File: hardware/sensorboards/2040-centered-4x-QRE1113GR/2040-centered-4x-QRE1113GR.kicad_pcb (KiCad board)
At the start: 2 copper layers, 49 x 46.5 mm, 15 parts, among them J1 Conn_01x10_Male, U1 QRE1113GR, U2 QRE1113GR, U3 QRE1113GR, U4 QRE1113GR

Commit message: removed extrusion which has nothing to do here in KiCad, will use OpenSCAD for rendering
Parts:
- removed ?: , 
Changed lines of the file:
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@@
       (net 11 "Net-(TP2-Pad1)") (pinfunction "1") (pintype "passive"))
-  )
-  (footprint "" (layer "F.Cu")
-    (at 168.1 92.1)
-    (fp_text reference "" (at 0 0) (layer "F.SilkS")
-      (effects (font (size 1.27 1.27) (thickness 0.15)))
-    )
-    (fp_text value "" (at 0 0) (layer "F.SilkS")
-      (effects (font (size 1.27 1.27) (thickness 0.15)))
-    )
-    (pad "" np_thru_hole circle (at 0 0) (size 3.2 3.2) (drill 3.2) (layers *.Cu *.Mask))
-    (model "/home/davide/repo/github/piano-conversion-davide/HFS5-4040-100.stp"
-      (offset (xyz -75 0 -22))
-      (scale (xyz 1 1 1))
-      (rotate (xyz 0 90 0))
-    )
   )
   (footprint "Mounting_Holes:MountingHole_3.2mm_M3" (layer "F.Cu")

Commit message: larger board for back action
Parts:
- moved J1 6.20 mm to (150.0, 62.1)
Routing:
- net /C4: track 28.9 -> 35.7 mm
- net Net-(U2-Pad3): track 27.6 -> 34.3 mm
- net /POS: track 39.3 -> 45.8 mm
- net /E3: track 27.6 -> 34.1 mm
- net /E2: track 24.6 -> 30.8 mm
- net /E1: track 28.9 -> 35.1 mm
- net /NEG: track 39.1 -> 45.2 mm
- net /C3: track 24.7 -> 30.8 mm
- net /C1: track 28.3 -> 34.0 mm
- net /E4: track 28.4 -> 34.0 mm
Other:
- board size 49 x 46.5 mm -> 49 x 52 mm
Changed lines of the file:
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@@
   )
   (footprint "Connector_PinHeader_2.54mm:PinHeader_1x10_P2.54mm_Vertical" (layer "B.Cu")
-    (at 149.96 68.3 90)
+    (at 149.96 62.1 90)
     (descr "Through hole straight pin header, 1x10, 2.54mm pitch, single row")
     (tags "Through hole pin header THT 1x10 2.54mm single row")
@@
     )
   )
-  (gr_rect (start 114 65.5) (end 163 112) (layer "Edge.Cuts") (width 0.05) (fill none))
-  (segment (start 149.96 68.3) (end 162 68.3) (width 1) (layer "F.Cu") (net 1))
-  (segment (start 162 68.3) (end 162 91) (width 1) (layer "F.Cu") (net 1))
-  (segment (start 162 91) (end 162 92.8) (width 1) (layer "F.Cu") (net 1))
+  (gr_rect (start 114 60) (end 163 112) (layer "Edge.Cuts") (width 0.05) (fill none))
+  (segment (start 162 62.2) (end 162 92.8) (width 1) (layer "F.Cu") (net 1))
+  (segment (start 161.9 62.1) (end 162 62.2) (width 0.25) (layer "F.Cu") (net 1))
+  (segment (start 149.96 62.1) (end 161.9 62.1) (width 1) (layer "F.Cu") (net 1))
   (segment (start 159.5 92.9) (end 161.9 92.9) (width 0.5) (layer "F.Cu") (net 1))
   (segment (start 161.9 92.9) (end 162 92.8) (width 0.5) (layer "F.Cu") (net 1))
-  (segment (start 155.8 90.8) (end 155.8 77.66927) (width 0.5) (layer "F.Cu") (net 2))
-  (segment (start 146.464635 69.884635) (end 144.88 68.3) (width 0.5) (layer "F.Cu") (net 2))
-  (segment (start 155.8 77.66927) (end 148.015365 69.884635) (width 0.5) (layer "F.Cu") (net 2))
-  (segment (start 148.015365 69.884635) (end 146.464635 69.884635) (width 0.5) (layer "F.Cu") (net 2))
-  (segment (start 155.5 91.1) (end 155.8 90.8) (width 0.5) (layer "F.Cu") (net 2))
+  (segment (start 155.8 90.8) (end 155.5 91.1) (width 0.5) (layer "F.Cu") (net 2))
+  (segment (start 155.8 72.4) (end 155.8 90.8) (width 0.5) (layer "F.Cu") (net 2))
+  (segment (start 145.5 62.1) (end 155.8 72.4) (width 0.5) (layer "F.Cu") (net 2))
+  (segment (start 144.88 62.1) (end 145.5 62.1) (width 0.5) (layer "F.Cu") (net 2))
   (segment (start 157.59952 91.1) (end 159.5 91.1) (width 0.5) (layer "F.Cu") (net 3))
-  (segment (start 147.42 68.3) (end 156.49952 77.37952) (width 0.5) (layer "F.Cu") (net 3))
+  (segment (start 156.5 77.37904) (end 156.49952 77.37952) (width 0.5) (layer "F.Cu") (net 3))
+  (segment (start 147.42 62.1) (end 147 62.1) (width 0.5) (layer "F.Cu") (net 3))
   (segment (start 156.49952 77.37952) (end 156.49952 90) (width 0.5) (layer "F.Cu") (net 3))
   (segment (start 156.49952 90) (end 157.59952 91.1) (width 0.5) (layer "F.Cu") (net 3))
+  (segment (start 147 62.1) (end 156.5 71.6) (width 0.5) (layer "F.Cu") (net 3))
+  (segment (start 156.5 71.6) (end 156.5 77.37904) (width 0.5) (layer "F.Cu") (net 3))
+  (segment (start 144.7 91.1) (end 142.9 91.1) (width 0.5) (layer "F.Cu") (net 4))
+  (segment (start 139.8 62.1) (end 140.2 62.1) (width 0.5) (layer "F.Cu") (net 4))
+  (segment (start 145.90048 67.80048) (end 145.90048 89.89952) (width 0.5) (layer "F.Cu") (net 4))
+  (segment (start 140.2 62.1) (end 145.90048 67.80048) (width 0.5) (layer "F.Cu") (net 4))
   (segment (start 145.90048 89.89952) (end 144.7 91.1) (width 0.5) (layer "F.Cu") (net 4))
-  (segment (start 145.90048 74.40048) (end 139.8 68.3) (width 0.5) (layer "F.Cu") (net 4))
-  (segment (start 144.7 91.1) (end 142.9 91.1) (width 0.5) (layer "F.Cu") (net 4))
-  (segment (start 145.90048 74.40048) (end 145.90048 89.89952) (width 0.5) (layer "F.Cu") (net 4))
-  (segment (start 142.34 69.84) (end 146.6 74.1) (width 0.5) (layer "F.Cu") (net 5))
-  (segment (start 142.34 68.3) (end 142.34 69.84) (width 0.5) (layer "F.Cu") (net 5))
+  (segment (start 146.6 67.4) (end 146.6 90.8) (width 0.5) (layer "F.Cu") (net 5))
   (segment (start 146.6 90.8) (end 146.9 91.1) (width 0.5) (layer "F.Cu") (net 5))
-  (segment (start 146.6 74.1) (end 146.6 90.8) (width 0.5) (layer "F.Cu") (net 5))
-  (segment (start 130.6 90.8) (end 130.6 73.97073) (width 0.5) (layer "F.Cu") (net 6))
-  (segment (start 134.72 69.85073) (end 134.72 68.3) (width 0.5) (layer "F.Cu") (net 6))
-  (segment (start 130.6 73.97073) (end 134.72 69.85073) (width 0.5) (layer "F.Cu") (net 6))
+  (segment (start 141.7 62.5) (end 146.6 67.4) (width 0.5) (layer "F.Cu") (net 5))
+  (segment (start 130.6 90.8) (end 130.6 67) (width 0.5) (layer "F.Cu") (net 6))
+  (segment (start 134.72 62.88) (end 134.72 62.1) (width 0.5) (layer "F.Cu") (net 6))
   (segment (start 130.3 91.1) (end 130.6 90.8) (width 0.5) (layer "F.Cu") (net 6))
-  (segment (start 129.64 68.3) (end 120.700481 77.239519) (width 0.5) (layer "F.Cu") (net 7))
+  (segment (start 130.6 67) (end 134.72 62.88) (width 0.5) (layer "F.Cu") (net 6))
+  (segment (start 129.64 62.1) (end 129.64 62.97073) (width 0.5) (layer "F.Cu") (net 7))
+  (segment (start 129.64 62.97073) (end 120.700481 71.910249) (width 0.5) (layer "F.Cu") (net 7))
   (segment (start 120.700481 89.999519) (end 119.6 91.1) (width 0.5) (layer "F.Cu") (net 7))
-  (segment (start 120.700481 77.239519) (end 120.700481 89.999519) (width 0.5) (layer "F.Cu") (net 7))
+  (segment (start 120.700481 71.910249) (end 120.700481 89.999519) (width 0.5) (layer "F.Cu") (net 7))
   (segment (start 119.6 91.1) (end 117.7 91.1) (width 0.5) (layer "F.Cu") (net 7))
-  (segment (start 129.114635 69.814635) (end 121.4 77.52927) (width 0.5) (layer "F.Cu") (net 8))
+  (segment (start 132.18 62.1) (end 131.5 62.1) (width 0.5) (layer "F.Cu") (net 8))
   (segment (start 121.4 90.8) (end 121.7 91.1) (width 0.5) (layer "F.Cu") (net 8))
   (segment (start 121.4 77.52927) (end 121.4 90.8) (width 0.5) (layer "F.Cu") (net 8))
-  (segment (start 130.665365 69.814635) (end 129.114635 69.814635) (width 0.5) (layer "F.Cu") (net 8))
-  (segment (start 132.18 68.3) (end 130.665365 69.814635) (width 0.5) (layer "F.Cu") (net 8))
+  (segment (start 131.5 62.1) (end 121.4 72.2) (width 0.5) (layer "F.Cu") (net 8))
+  (segment (start 121.4 72.2) (end 121.4 77.52927) (width 0.5) (layer "F.Cu") (net 8))
   (segment (start 115 92.9) (end 117.7 92.9) (width 0.5) (layer "F.Cu") (net 9))
-  (segment (start 115.1 68.3) (end 127.1 68.3) (width 1) (layer "F.Cu") (net 9))
-  (segment (start 115 68.4) (end 115.1 68.3) (width 1) (layer "F.Cu") (net 9))
+  (segment (start 115 62.1) (end 115 68.6) (width 1) (layer "F.Cu") (net 9))
   (segment (start 115 91) (end 115 92.9) (width 1) (layer "F.Cu") (net 9))
   (segment (start 115 91) (end 115 68.4) (width 1) (layer "F.Cu") (net 9))
+  (segment (start 127.1 62.1) (end 115 62.1) (width 1) (layer "F.Cu") (net 9))
   (segment (start 119 108) (end 119 99.7) (width 0.5) (layer "F.Cu") (net 10))
   (segment (start 119 99.7) (end 125.8 92.9) (width 0.5) (layer "F.Cu") (net 10))
@@
   (segment (start 146.9 92.9) (end 155.5 92.9) (width 0.5) (layer "F.Cu") (net 12))
   (segment (start 158 99.7) (end 151.2 92.9) (width 0.5) (layer "F.Cu") (net 12))
-  (segment (start 131.29952 74.26048) (end 131.29952 90) (width 0.5) (layer "F.Cu") (net 13))
+  (segment (start 131.29952 90) (end 132.39952 91.1) (width 0.5) (layer "F.Cu") (net 13))
+  (segment (start 135.189759 63.399511) (end 135.258276 63.399511) (width 0.5) (layer "F.Cu") (net 13))
+  (segment (start 136.5 62.1) (end 137.26 62.1) (width 0.5) (layer "F.Cu") (net 13))
+  (segment (start 135.189759 63.399511) (end 131.29952 67.28975) (width 0.5) (layer "F.Cu") (net 13))
+  (segment (start 136 62.6) (end 136.5 62.1) (width 0.5) (layer "F.Cu") (net 13))
   (segment (start 132.39952 91.1) (end 134.3 91.1) (width 0.5) (layer "F.Cu") (net 13))
-  (segment (start 137.26 68.3) (end 131.29952 74.26048) (width 0.5) (layer "F.Cu") (net 13))
-  (segment (start 131.29952 90) (end 132.39952 91.1) (width 0.5) (layer "F.Cu") (net 13))
+  (segment (start 135.258276 63.399511) (end 136 62.657787) (width 0.5) (layer "F.Cu") (net 13))
+  (segment (start 136 62.657787) (end 136 62.6) (width 0.5) (layer "F.Cu") (net 13))
+  (segment (start 131.29952 67.28975) (end 131.29952 90) (width 0.5) (layer "F.Cu") (net 13))
 )

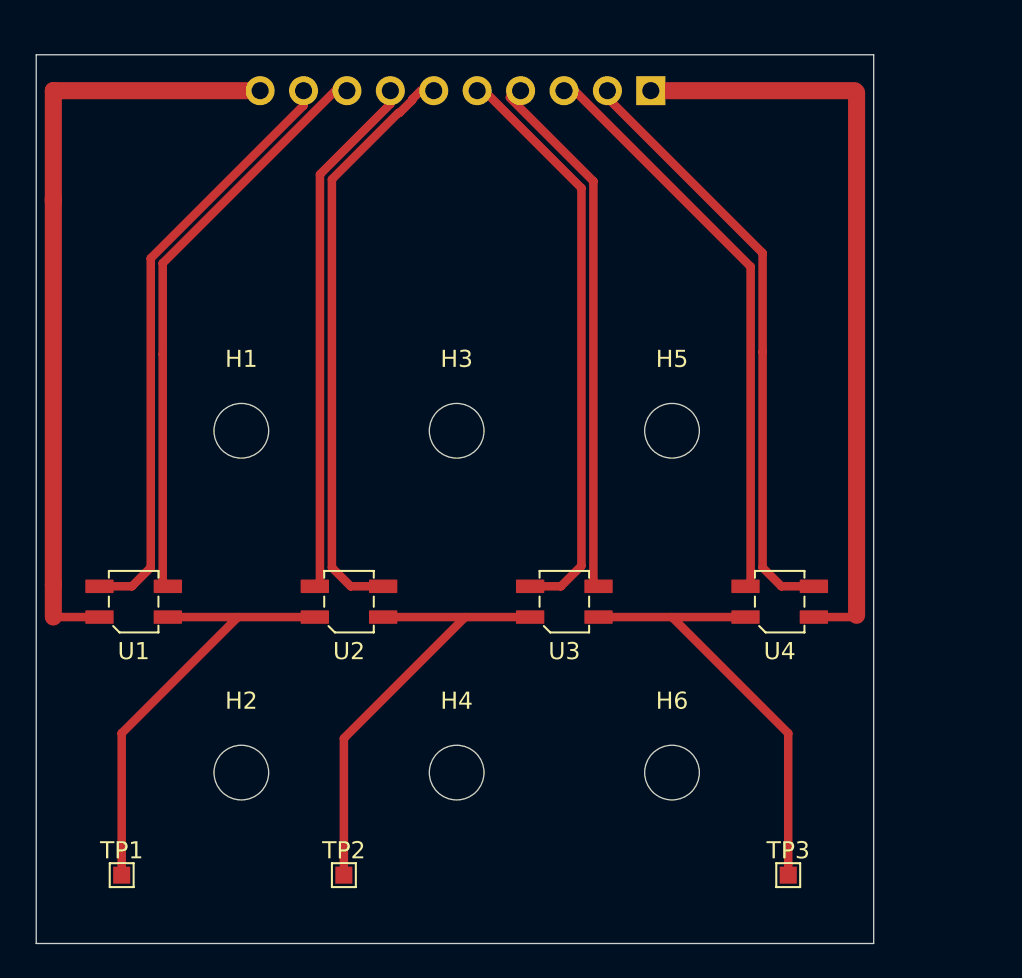
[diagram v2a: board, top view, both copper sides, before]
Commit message: align guide lines, labels next to the connector and thicker footprint, all on the silkscreen
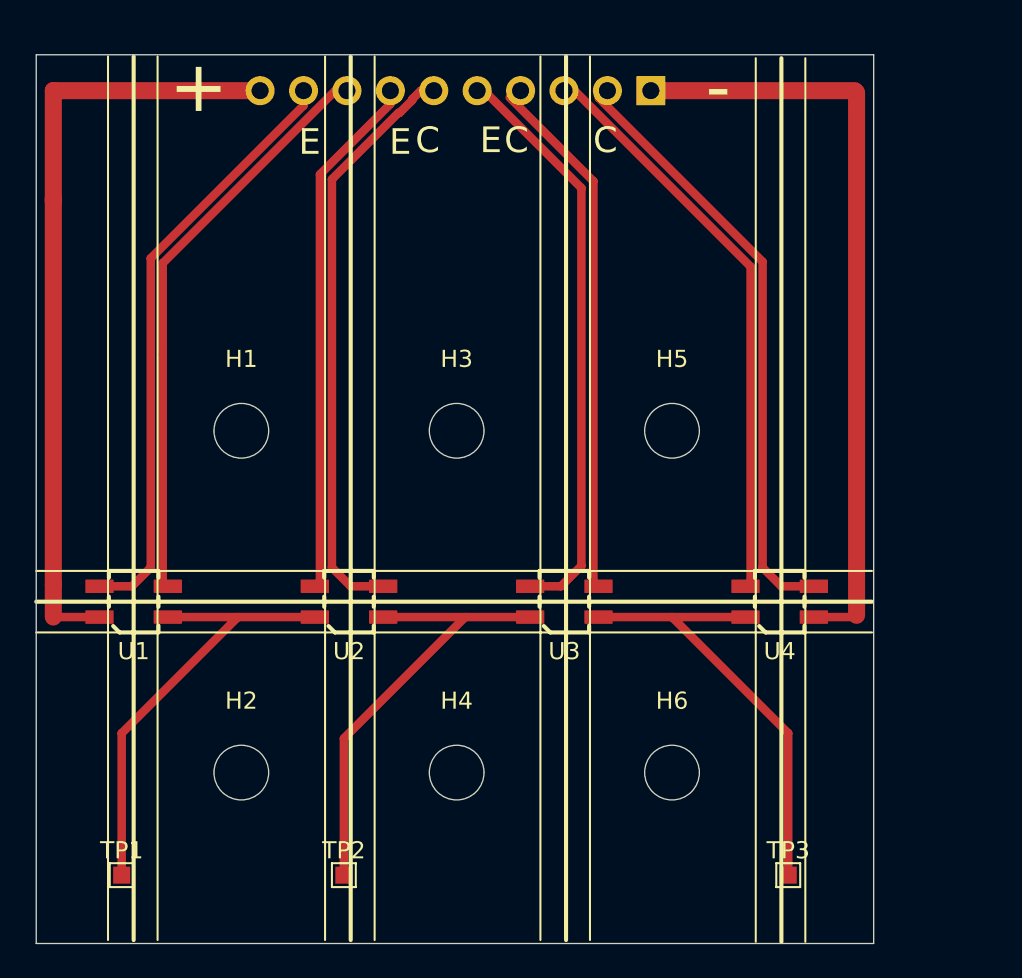
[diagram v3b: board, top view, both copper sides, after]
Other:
- board text added: "+"
- board text added: "-"
- board text added: "C"
- board text added: "E"

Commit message: board revision and info, removed some silkscreen overlap violations
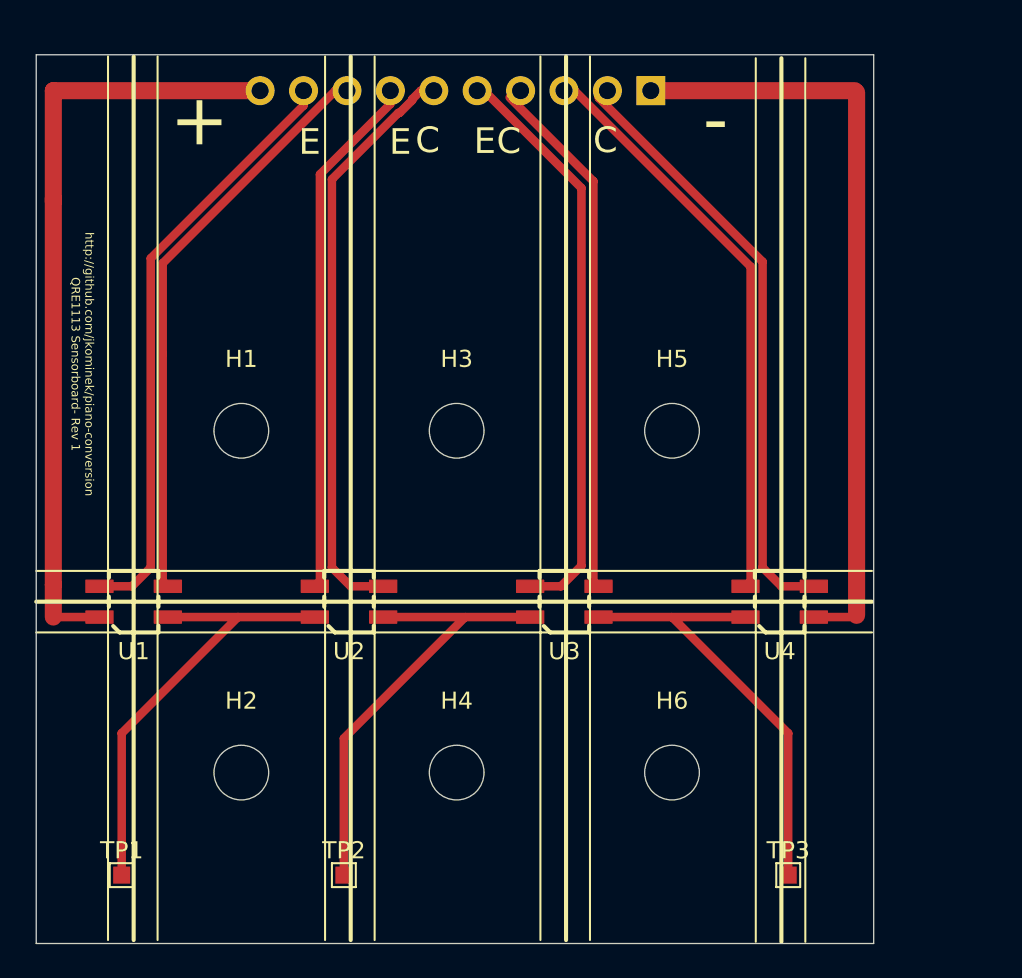
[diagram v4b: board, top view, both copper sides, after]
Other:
- board text added: "http://github.com/jkominek/piano-conversion QRE1113 Sensorboard- Rev 1"
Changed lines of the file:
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@@
   )
   (setup
+    (stackup
+      (layer "F.SilkS" (type "Top Silk Screen"))
+      (layer "F.Paste" (type "Top Solder Paste"))
+      (layer "F.Mask" (type "Top Solder Mask") (thickness 0.01))
+      (layer "F.Cu" (type "copper") (thickness 0.035))
+      (layer "dielectric 1" (type "core") (thickness 1.51) (material "FR4") (epsilon_r 4.5) (loss_tangent 0.02))
+      (layer "B.Cu" (type "copper") (thickness 0.035))
+      (layer "B.Mask" (type "Bottom Solder Mask") (thickness 0.01))
+      (layer "B.Paste" (type "Bottom Solder Paste"))
+      (layer "B.SilkS" (type "Bottom Silk Screen"))
+      (copper_finish "None")
+      (dielectric_constraints no)
+    )
     (pad_to_mask_clearance 0)
     (pcbplotparams
@@
   (gr_line (start 146.4 60.1) (end 146.4 111.8) (layer "F.SilkS") (width 0.12))
   (gr_rect (start 114 60) (end 163 112) (layer "Edge.Cuts") (width 0.05) (fill none))
-  (gr_text "-" (at 153.9 61.9) (layer "F.SilkS")
+  (gr_text "-" (at 153.75 63.8) (layer "F.SilkS")
     (effects (font (size 3 3) (thickness 0.5)))
   )
-  (gr_text "C" (at 142.1 65) (layer "F.SilkS")
+  (gr_text "C" (at 141.65 65.05) (layer "F.SilkS")
     (effects (font (size 1.5 1.5) (thickness 0.25)))
   )
@@
     (effects (font (size 1.5 1.5) (thickness 0.25)))
   )
-  (gr_text "+" (at 123.5 61.9) (layer "F.SilkS")
+  (gr_text "+" (at 123.55 63.85) (layer "F.SilkS")
     (effects (font (size 3 3) (thickness 0.5)))
   )
-  (gr_text "E" (at 140.6 65) (layer "F.SilkS")
+  (gr_text "http://github.com/jkominek/piano-conversion\nQRE1113 Sensorboard- Rev 1" (at 116.7 78.1 -90) (layer "F.SilkS")
+    (effects (font (size 0.5 0.5) (thickness 0.1)))
+  )
+  (gr_text "E" (at 140.25 65.05) (layer "F.SilkS")
     (effects (font (size 1.5 1.5) (thickness 0.25)))
   )
